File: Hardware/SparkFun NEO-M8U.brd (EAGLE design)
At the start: 40.6 x 33 mm, 98 parts, among them J3 Qwiic Right Angle, J4 Qwiic Right Angle, J7 U.FL, U1 U-BLOX_MEO-M8U, U2 3.3V

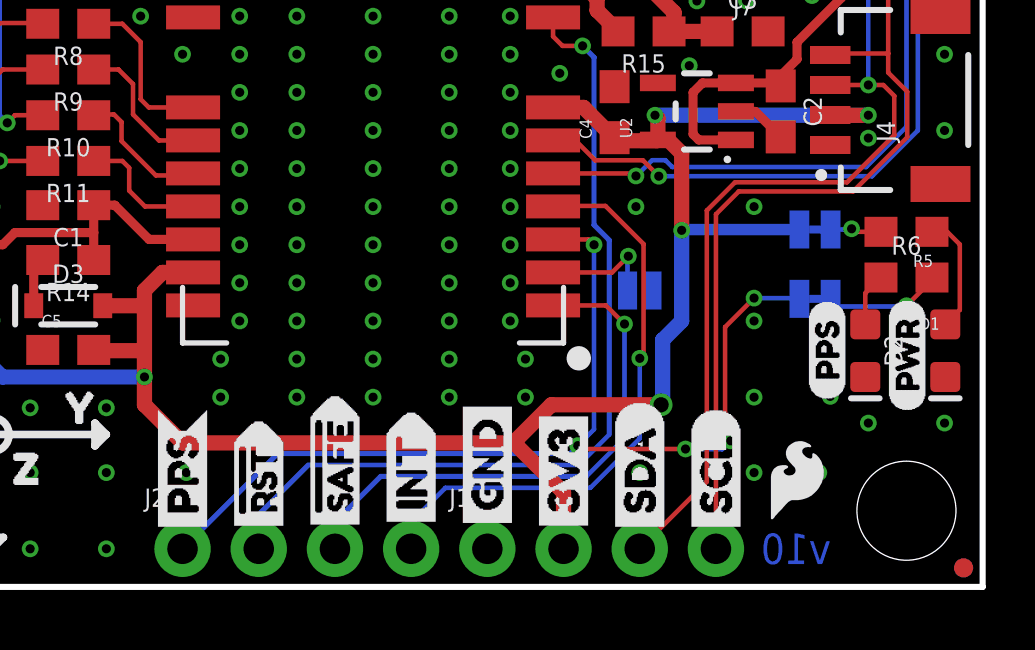
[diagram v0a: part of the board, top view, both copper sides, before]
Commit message: Adjusts some wonky trace widths, moves some traces for better pour
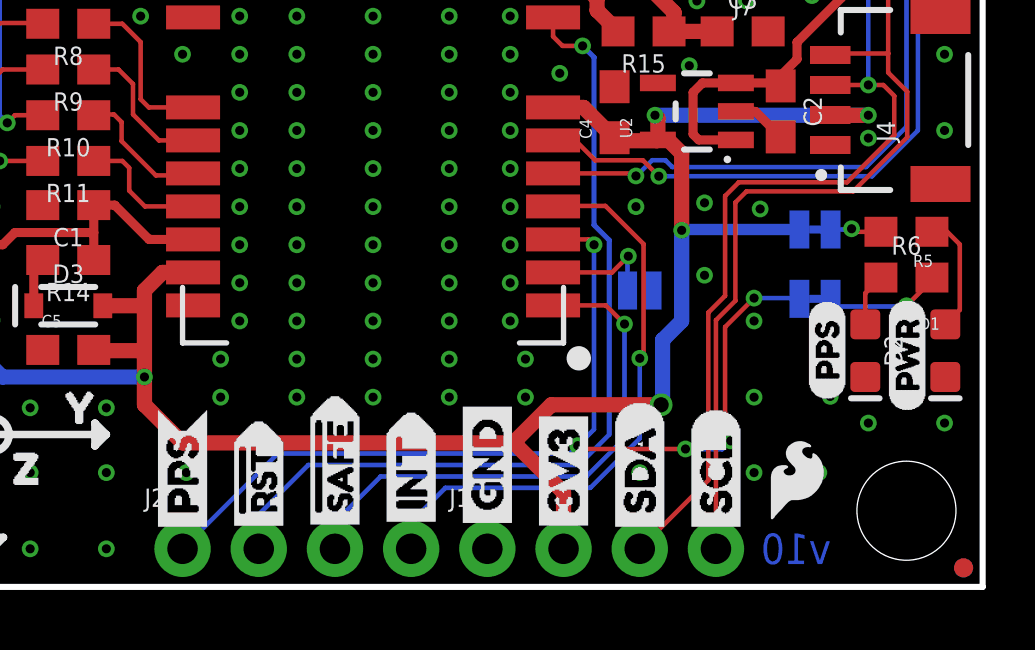
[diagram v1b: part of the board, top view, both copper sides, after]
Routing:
- net GND: vias 153 -> 155
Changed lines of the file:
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@@
 <setting verticaltext="up"/>
 </settings>
-<grid distance="0.05" unitdist="inch" unit="inch" style="lines" multiple="1" display="yes" altdistance="0.005" altunitdist="inch" altunit="inch"/>
+<grid distance="0.05" unitdist="inch" unit="inch" style="lines" multiple="1" display="yes" altdistance="0.002" altunitdist="inch" altunit="inch"/>
 <layers>
 <layer number="1" name="Top" color="4" fill="1" visible="yes" active="yes"/>
@@
 <contactref element="C3" pad="2"/>
 <via x="6.35" y="17.7546" extent="1-16" drill="0.3048"/>
-<via x="33.02" y="12.6746" extent="1-16" drill="0.3048"/>
+<via x="33.2232" y="12.5984" extent="1-16" drill="0.3048"/>
 <via x="15.875" y="8.8646" extent="1-16" drill="0.3048"/>
 <via x="17.78" y="8.8646" extent="1-16" drill="0.3048"/>
@@
 <via x="15.24" y="7.5946" extent="1-16" drill="0.3048"/>
 <via x="7.62" y="8.89" extent="1-16" drill="0.3048"/>
+<via x="31.369" y="12.8016" extent="1-16" drill="0.3048"/>
+<via x="31.369" y="10.3886" extent="1-16" drill="0.3048"/>
 </signal>
 <signal name="SCL/SCK">
@@
 <contactref element="R9" pad="2"/>
 <wire x1="5.08" y1="14.7306" x2="6.374" y2="14.7306" width="0.1524" layer="1"/>
-<wire x1="31.75" y1="12.4206" x2="32.512" y2="13.1826" width="0.1524" layer="1"/>
-<wire x1="32.512" y1="13.1826" x2="36.322" y2="13.1826" width="0.1524" layer="1"/>
+<wire x1="32.3977" y1="12.8143" x2="32.766" y2="13.1826" width="0.1524" layer="1"/>
+<wire x1="32.766" y1="13.1826" x2="36.322" y2="13.1826" width="0.1524" layer="1"/>
 <wire x1="36.322" y1="13.1826" x2="38.12578125" y2="14.98638125" width="0.1524" layer="1"/>
 <wire x1="38.12578125" y1="14.98638125" x2="38.12578125" y2="16.51" width="0.1524" layer="1"/>
@@
 <contactref element="J6" pad="7"/>
 <contactref element="J1" pad="4"/>
-<wire x1="31.75" y1="1.27" x2="31.75" y2="12.4206" width="0.1524" layer="1"/>
 <via x="5.8180875" y="19.3802" extent="1-16" drill="0.3048"/>
 <contactref element="R4" pad="1"/>
@@
 <wire x1="7.747" y1="17.018" x2="7.9756" y2="17.2466" width="0.1524" layer="1"/>
 <wire x1="7.9756" y1="17.2466" x2="9.31" y2="17.2466" width="0.1524" layer="1"/>
+<wire x1="31.75" y1="1.27" x2="31.75" y2="8.89" width="0.1524" layer="1"/>
+<wire x1="32.3977" y1="9.5377" x2="32.3977" y2="12.8143" width="0.1524" layer="1"/>
+<wire x1="31.75" y1="8.89" x2="32.3977" y2="9.5377" width="0.1524" layer="1"/>
 </signal>
 <signal name="SDA/!CS">
@@
 <contactref element="R8" pad="2"/>
 <wire x1="9.144" y1="18.7706" x2="9.31" y2="18.7706" width="0.1524" layer="1"/>
-<wire x1="31.4452" y1="12.54685625" x2="31.4452" y2="3.5052" width="0.1524" layer="1"/>
 <wire x1="36.11954375" y1="13.4874" x2="37.69396875" y2="15.061825" width="0.1524" layer="1"/>
-<wire x1="31.4452" y1="12.54685625" x2="32.38574375" y2="13.4874" width="0.1524" layer="1"/>
-<wire x1="32.38574375" y1="13.4874" x2="36.11954375" y2="13.4874" width="0.1524" layer="1"/>
+<wire x1="32.055171875" y1="13.029828125" x2="32.51274375" y2="13.4874" width="0.1524" layer="1"/>
+<wire x1="32.51274375" y1="13.4874" x2="36.11954375" y2="13.4874" width="0.1524" layer="1"/>
 <wire x1="36.83" y1="16.7306" x2="35.56" y2="16.7306" width="0.1524" layer="1"/>
 <wire x1="6.35" y1="18.7706" x2="4.191" y2="18.7706" width="0.1524" layer="1"/>
@@
 <wire x1="37.18598125" y1="20.39658125" x2="37.18598125" y2="25.1206" width="0.1524" layer="1"/>
 <contactref element="J1" pad="3"/>
-<wire x1="31.4452" y1="3.5052" x2="29.21" y2="1.27" width="0.1524" layer="1"/>
 <wire x1="37.69396875" y1="15.061825" x2="37.69396875" y2="16.366628125" width="0.1524" layer="1"/>
 <wire x1="5.08" y1="15.7306" x2="4.056" y2="15.7306" width="0.1524" layer="1"/>
@@
 <wire x1="6.9676" y1="15.7306" x2="7.493" y2="16.256" width="0.1524" layer="1"/>
 <wire x1="7.493" y1="16.256" x2="7.493" y2="18.415" width="0.1524" layer="1"/>
+<wire x1="32.055171875" y1="9.703171875" x2="32.055171875" y2="13.029828125" width="0.1524" layer="1"/>
+<wire x1="29.21" y1="1.27" x2="31.496" y2="3.556" width="0.1524" layer="1"/>
+<wire x1="31.496" y1="3.556" x2="31.496" y2="9.144" width="0.1524" layer="1"/>
+<wire x1="31.496" y1="9.144" x2="32.055171875" y2="9.703171875" width="0.1524" layer="1"/>
 </signal>
 <signal name="PPS">
@@
 <wire x1="26.32" y1="11.583" x2="27.5076" y2="11.583" width="0.1524" layer="1"/>
 <wire x1="27.5076" y1="11.583" x2="27.686" y2="11.4046" width="0.1524" layer="1"/>
-<wire x1="13.97" y1="1.27" x2="17.145" y2="4.445" width="0.17" layer="16"/>
-<wire x1="17.145" y1="4.445" x2="26.8801125" y2="4.445" width="0.17" layer="16"/>
+<wire x1="13.97" y1="1.27" x2="17.145" y2="4.445" width="0.1524" layer="16"/>
+<wire x1="17.145" y1="4.445" x2="26.8801125" y2="4.445" width="0.1524" layer="16"/>
 <wire x1="34.5186" y1="9.6266" x2="34.5313" y2="9.6139" width="0.1524" layer="16"/>
 <wire x1="34.5313" y1="9.6139" x2="34.5313" y2="9.6012" width="0.1524" layer="16"/>
@@
 <contactref element="U1" pad="8"/>
 <contactref element="J2" pad="2"/>
-<wire x1="16.51" y1="1.27" x2="16.51" y2="2.413" width="0.17" layer="16"/>
-<wire x1="18.161" y1="4.064" x2="16.51" y2="2.413" width="0.17" layer="16"/>
+<wire x1="16.51" y1="1.27" x2="16.51" y2="2.413" width="0.1524" layer="16"/>
+<wire x1="18.161" y1="4.064" x2="16.51" y2="2.413" width="0.1524" layer="16"/>
 <wire x1="28.194" y1="5.08" x2="28.194" y2="11.557" width="0.17" layer="16"/>
 <wire x1="28.194" y1="11.557" x2="27.686" y2="12.065" width="0.17" layer="16"/>
@@
 <contactref element="U1" pad="1"/>
 <contactref element="J2" pad="3"/>
-<wire x1="20.574" y1="3.683" x2="19.05" y2="2.159" width="0.17" layer="16"/>
-<wire x1="19.05" y1="1.27" x2="19.05" y2="2.159" width="0.17" layer="16"/>
+<wire x1="20.574" y1="3.683" x2="19.05" y2="2.159" width="0.1524" layer="16"/>
+<wire x1="19.05" y1="1.27" x2="19.05" y2="2.159" width="0.1524" layer="16"/>
 <wire x1="28.702" y1="4.953" x2="28.702" y2="8.763" width="0.1524" layer="16"/>
 <via x="28.702" y="8.763" extent="1-16" drill="0.3048"/>
@@
 <wire x1="28.082" y1="9.383" x2="26.32" y2="9.383" width="0.1524" layer="1"/>
 <wire x1="27.432" y1="3.683" x2="28.702" y2="4.953" width="0.1524" layer="16"/>
-<wire x1="20.574" y1="3.683" x2="27.432" y2="3.683" width="0.17" layer="16"/>
+<wire x1="20.574" y1="3.683" x2="27.432" y2="3.683" width="0.1524" layer="16"/>
 </signal>
 <signal name="N$3">
